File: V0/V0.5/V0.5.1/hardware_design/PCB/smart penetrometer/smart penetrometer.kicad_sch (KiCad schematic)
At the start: 46 parts, among them J1 Conn_01x02_Female, J2 XLR3_Switched, J3 Conn_01x07_Female, J4 Screw_Terminal, J5 Conn_02x04, U1 ADS1120IRVAR, U2 DS3231M, U3 BME260, U4 ADS1118IDGS, U5 VO615A

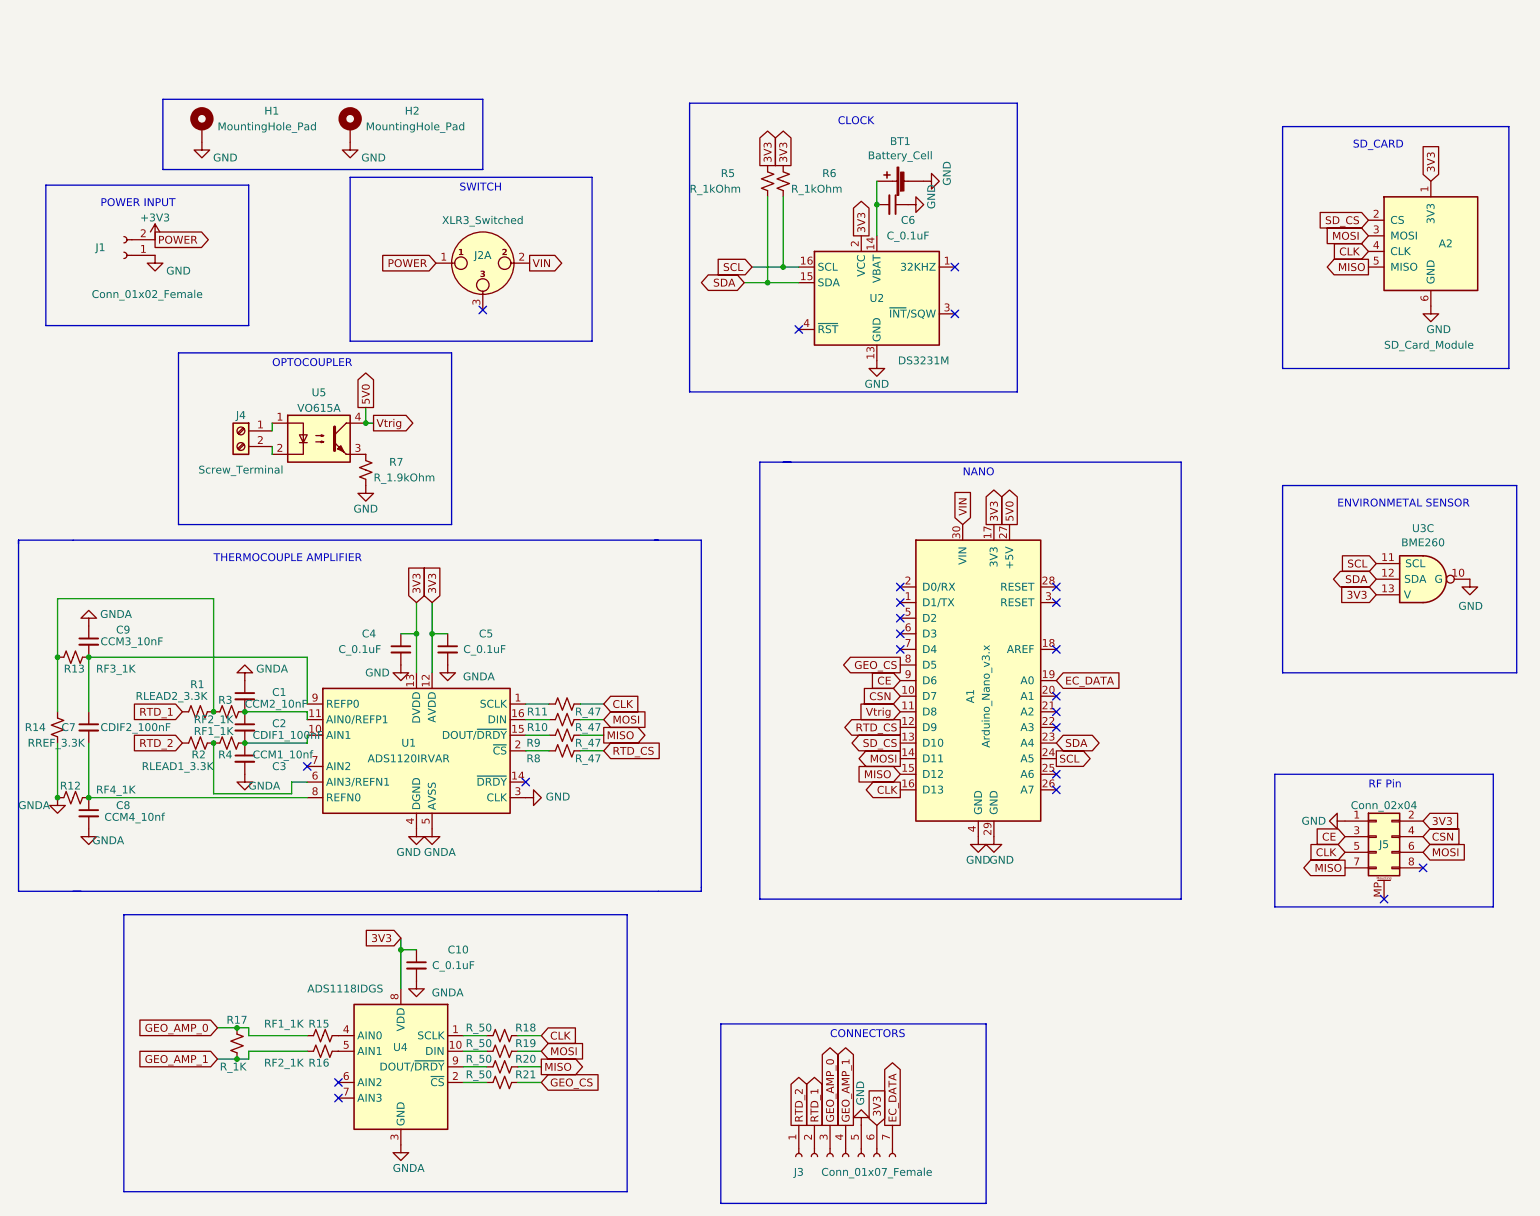
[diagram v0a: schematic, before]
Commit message: reorganized folders
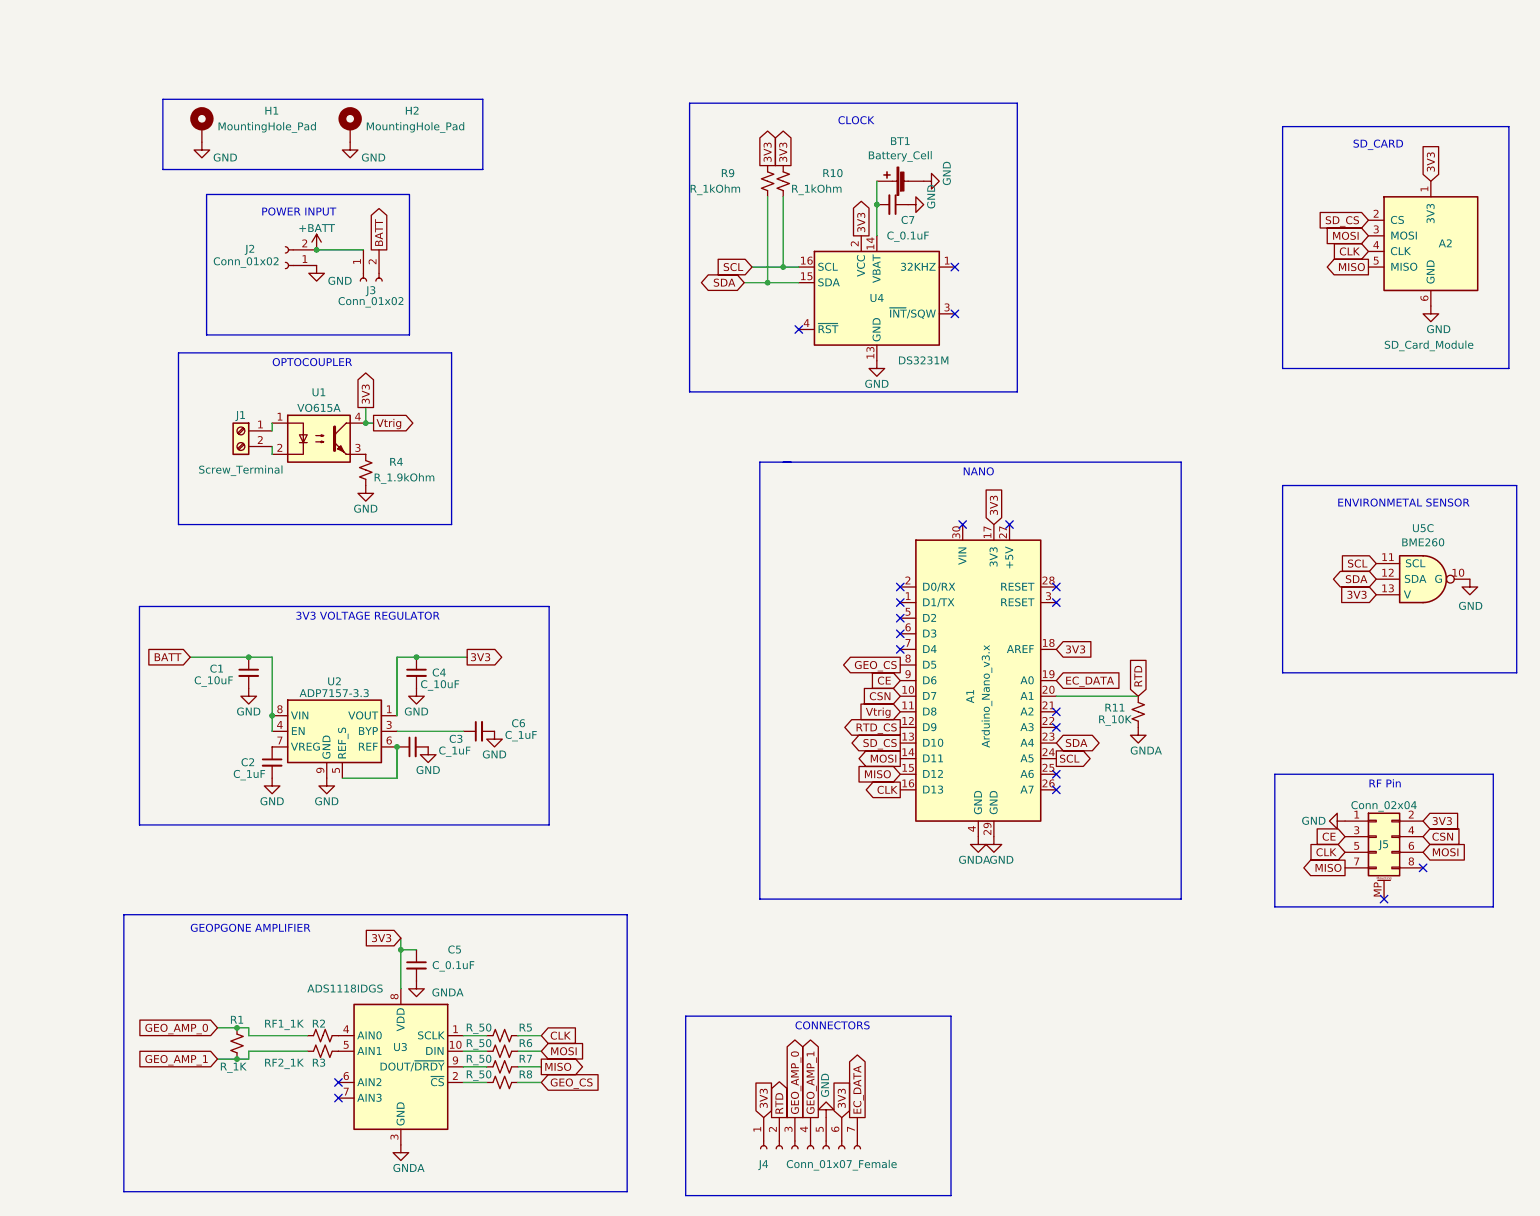
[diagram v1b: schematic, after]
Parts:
- removed C5: C_0.1uF, Capacitor_SMD:C_1206_3216Metric, symbol Device:C_Small
- removed C7: CDIF2_100nF, Capacitor_SMD:C_1206_3216Metric, symbol Device:C_Small
- removed C8: CCM4_10nf, Capacitor_SMD:C_1206_3216Metric, symbol Device:C_Small
- removed C9: CCM3_10nF, Capacitor_SMD:C_1206_3216Metric, symbol Device:C_Small
- removed J2: XLR3_Switched, kitest:grounded_switch, symbol Connector:XLR3_Switched
- removed R1: RLEAD2_3.3K, Resistor_SMD:R_1206_3216Metric, symbol Device:R_Small_US
- removed R10, R8, R9: R_47, Resistor_SMD:R_1206_3216Metric, symbol Device:R_Small_US
- removed R12: RF4_1K, Resistor_SMD:R_1206_3216Metric, symbol Device:R_Small_US
- removed R13: RF3_1K, Resistor_SMD:R_1206_3216Metric, symbol Device:R_Small_US
- removed R14: RREF_3.3K, Resistor_SMD:R_1206_3216Metric, symbol Device:R_Small_US
- removed R2: RLEAD1_3.3K, Resistor_SMD:R_1206_3216Metric, symbol Device:R_Small_US
- removed R3: RF2_1K, Resistor_SMD:R_1206_3216Metric, symbol Device:R_Small_US
- removed R4: RF1_1K, Resistor_SMD:R_1206_3216Metric, symbol Device:R_Small_US
- removed U1: ADS1120IRVAR, kitest:ADS1120IPW 16TSSOP, symbol Analog_ADC:ADS1120-PW
- added C6: C_1uF, Capacitor_SMD:C_1206_3216Metric, symbol Device:C_Small
- added J3: Conn_01x02, Connector_PinSocket_2.54mm:PinSocket_1x02_P2.54mm_Horizontal, symbol Connector:Conn_01x02_Female
- added U2: ADP7157-3.3, Package_SO:SOIC-8-1EP_3.9x4.9mm_P1.27mm_EP2.29x3mm, symbol Regulator_Linear:ADP7142ARDZ-3.3
- C1: value CCM2_10nF -> C_10uF
- C2: value CDIF1_100nF -> C_1uF
- C3: value CCM1_10nf -> C_1uF
- C4: value C_0.1uF -> C_10uF
- J2: renamed from J1; value Conn_01x02_Female -> Conn_01x02
- R11: value R_47 -> R_10K
- renumbered C10 to C5, C6 to C7, J4 to J1, J3 to J4, R17 to R1, R6 to R10, R15 to R2, R16 to R3, R7 to R4, R18 to R5, R19 to R6, R20 to R7, R21 to R8, R5 to R9, U5 to U1, U4 to U3, U2 to U4, U3 to U5
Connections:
- net RTD_1 is gone; now on net RTD: J4.2 (Pin_2)
- net RTD_2 is gone; now on net 3V3: J4.1 (Pin_1)
- net 3V3: now also A1.11 (D8), A1.18 (AREF), U1.4, U2.1 (VOUT), U2.2 (VOUT)
- net CLK: no longer R11.1
- net GND: now also C1.2, C2.2, C3.2, C6.2, U2.9 (GND); no longer A1.4 (GND)
- net GNDA: now also A1.4 (GND), R11.2; no longer C1.1, C3.2
- net at C2.1: now also U2.7 (VREG); no longer C1.2
- net RTD: now reaches A1.20 (A1)
- net RTD: now also R11.1
- net at C3.1: now also U2.5 (REF_S), U2.6 (REF); no longer C2.2
- net +3V3 renamed +BATT
- net +BATT: now also J3.1 (Pin_1)
- removed net 5V0: A1.11 (D8), A1.27 (+5V), U1.4
- net VIN: no longer names the net of A1.30 (VIN)
- new net: C6.1, U2.3 (BYP)
- new net BATT: C1.1, J3.2 (Pin_2), U2.4 (EN), U2.8 (VIN)
- no-connect marks 23 -> 20
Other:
- note added: "3V3 VOLTAGE REGULATOR"
- note added: "GEOPGONE AMPLIFIER"
- note removed: "SWITCH"
- note removed: "THERMOCOUPLE AMPLIFIER"
- moved on the sheet: J2, J4

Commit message: update
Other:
- note added: "SMART PENETROMETER"
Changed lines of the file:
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@@
     (date "2023-05-05")
     (company "ARTS LAB")
+    (comment 1 "Designer: Malichi Flemming II")
   )
   (junction (at 59.055 116.205) (diameter 0) (color 0 0 0 0)
@@
     (stroke (width 0) (type default))
   )
-  (polyline (pts (xy 261.62 109.22) (xy 223.52 109.22))
+  (polyline (pts (xy 262.382 109.474) (xy 223.52 109.474))
     (stroke (width 0) (type default))
   )
@@
     (stroke (width 0) (type default))
   )
-  (polyline (pts (xy 223.52 78.74) (xy 223.52 109.22))
-    (stroke (width 0) (type default))
-  )
-  (polyline (pts (xy 261.62 78.74) (xy 261.62 109.22))
+  (polyline (pts (xy 222.504 78.74) (xy 222.504 109.22))
+    (stroke (width 0) (type default))
+  )
+  (polyline (pts (xy 262.382 78.994) (xy 262.382 109.474))
     (stroke (width 0) (type default))
   )
@@
     (stroke (width 0) (type default))
   )
-  (polyline (pts (xy 223.52 78.74) (xy 261.62 78.74))
+  (polyline (pts (xy 223.52 78.994) (xy 262.382 78.994))
     (stroke (width 0) (type default))
   )
@@
     (stroke (width 0) (type default))
     (fill (type none))
+  )
+  (text "SMART PENETROMETER" (at 93.472 11.684 0)
+    (effects (font (face "Arial Black") (size 6 6)) (justify left bottom))
   )
   (text "GEOPGONE AMPLIFIER" (at 45.72 151.765 0)
     (effects (font (size 1.27 1.27)) (justify left bottom))
   )
-  (text "POWER INPUT" (at 57.277 35.179 0)
-    (effects (font (size 1.27 1.27)) (justify left bottom))
-  )
-  (text "3V3 VOLTAGE REGULATOR" (at 62.865 100.965 0)
-    (effects (font (size 1.27 1.27)) (justify left bottom))
-  )
-  (text "NANO" (at 171.45 77.47 0)
-    (effects (font (size 1.27 1.27)) (justify left bottom))
-  )
-  (text "CLOCK" (at 151.13 20.32 0)
-    (effects (font (size 1.27 1.27)) (justify left bottom))
-  )
-  (text "RF Pin" (at 237.49 128.27 0)
-    (effects (font (size 1.27 1.27)) (justify left bottom))
-  )
-  (text "CONNECTORS" (at 144.145 167.64 0)
-    (effects (font (size 1.27 1.27)) (justify left bottom))
-  )
-  (text "SD_CARD" (at 234.95 24.13 0)
-    (effects (font (size 1.27 1.27)) (justify left bottom))
-  )
-  (text "ENVIRONMETAL SENSOR" (at 232.41 82.55 0)
-    (effects (font (size 1.27 1.27)) (justify left bottom))
-  )
-  (text "OPTOCOUPLER" (at 59.055 59.69 0)
-    (effects (font (size 1.27 1.27)) (justify left bottom))
+  (text "POWER INPUT" (at 53.848 35.306 0)
+    (effects (font (face "Arial Black") (size 2 2)) (justify left bottom))
+  )
+  (text "3V3 VOLTAGE REGULATOR" (at 51.308 103.124 0)
+    (effects (font (face "Arial Black") (size 2 2)) (justify left bottom))
+  )
+  (text "NANO" (at 167.132 79.502 0)
+    (effects (font (face "Arial Black") (size 2 2)) (justify left bottom))
+  )
+  (text "CLOCK" (at 147.828 21.336 0)
+    (effects (font (face "Arial Black") (size 2 2)) (justify left bottom))
+  )
+  (text "RF Pin" (at 233.934 129.794 0)
+    (effects (font (face "Arial Black") (size 2 2)) (justify left bottom))
+  )
+  (text "CONNECTORS" (at 137.16 168.91 0)
+    (effects (font (face "Arial Black") (size 2 2)) (justify left bottom))
+  )
+  (text "SD_CARD" (at 230.886 25.146 0)
+    (effects (font (face "Arial Black") (size 2 2)) (justify left bottom))
+  )
+  (text "ENVIRONMETAL SENSOR" (at 223.012 83.312 0)
+    (effects (font (face "Arial Black") (size 2 2)) (justify left bottom))
+  )
+  (text "OPTOCOUPLER" (at 49.276 61.468 0)
+    (effects (font (face "Arial Black") (size 2 2)) (justify left bottom))
   )
   (global_label "SDA" (shape bidirectional) (at 135.89 45.72 180) (fields_autoplaced)
@@
       (effects (font (size 1.27 1.27)) hide)
     )
-    (property "Value" "GND" (at 168.91 27.94 0)
+    (property "Value" "GND" (at 170.18 29.21 90)
       (effects (font (size 1.27 1.27)))
     )
@@
   (symbol (lib_id "Device:R_Small_US") (at 139.7 29.21 0) (unit 1)
     (in_bom yes) (on_board yes) (dnp no)
-    (property "Reference" "R9" (at 132.08 27.94 0)
-      (effects (font (size 1.27 1.27)) (justify left))
-    )
-    (property "Value" "R_1kOhm" (at 127 30.48 0)
+    (property "Reference" "R9" (at 133.096 28.194 0)
+      (effects (font (size 1.27 1.27)) (justify left))
+    )
+    (property "Value" "R_1kOhm" (at 129.54 30.226 0)
       (effects (font (size 1.27 1.27)) (justify left))
     )
@@
   (symbol (lib_id "Device:C_Small") (at 160.02 33.02 270) (unit 1)
     (in_bom yes) (on_board yes) (dnp no)
-    (property "Reference" "C7" (at 162.56 35.56 90)
-      (effects (font (size 1.27 1.27)))
-    )
-    (property "Value" "C_0.1uF" (at 162.56 38.1 90)
+    (property "Reference" "C7" (at 161.544 35.56 90)
+      (effects (font (size 1.27 1.27)))
+    )
+    (property "Value" "C_0.1uF" (at 161.798 37.592 90)
       (effects (font (size 1.27 1.27)))
     )
@@
       (effects (font (size 1.27 1.27)) hide)
     )
-    (property "Value" "GND" (at 166.37 31.75 0)
+    (property "Value" "GND" (at 167.386 33.274 90)
       (effects (font (size 1.27 1.27)))
     )
@@
   (symbol (lib_id "Device:R_Small_US") (at 142.24 29.21 0) (unit 1)
     (in_bom yes) (on_board yes) (dnp no)
-    (property "Reference" "R10" (at 148.59 27.94 0)
-      (effects (font (size 1.27 1.27)) (justify left))
-    )
+    (property "Reference" "R10" (at 146.05 28.194 0)
+      (effects (font (size 1.27 1.27)) (justify left))
+    )
